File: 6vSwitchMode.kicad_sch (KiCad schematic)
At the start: 29 parts, among them IC1 TPS40192DRCT-TPS40192DRCT, Q1 BUK9M17-30EX / BUK7M10-40E, Q2 BUK9M17-30EX / BUK7M10-40E

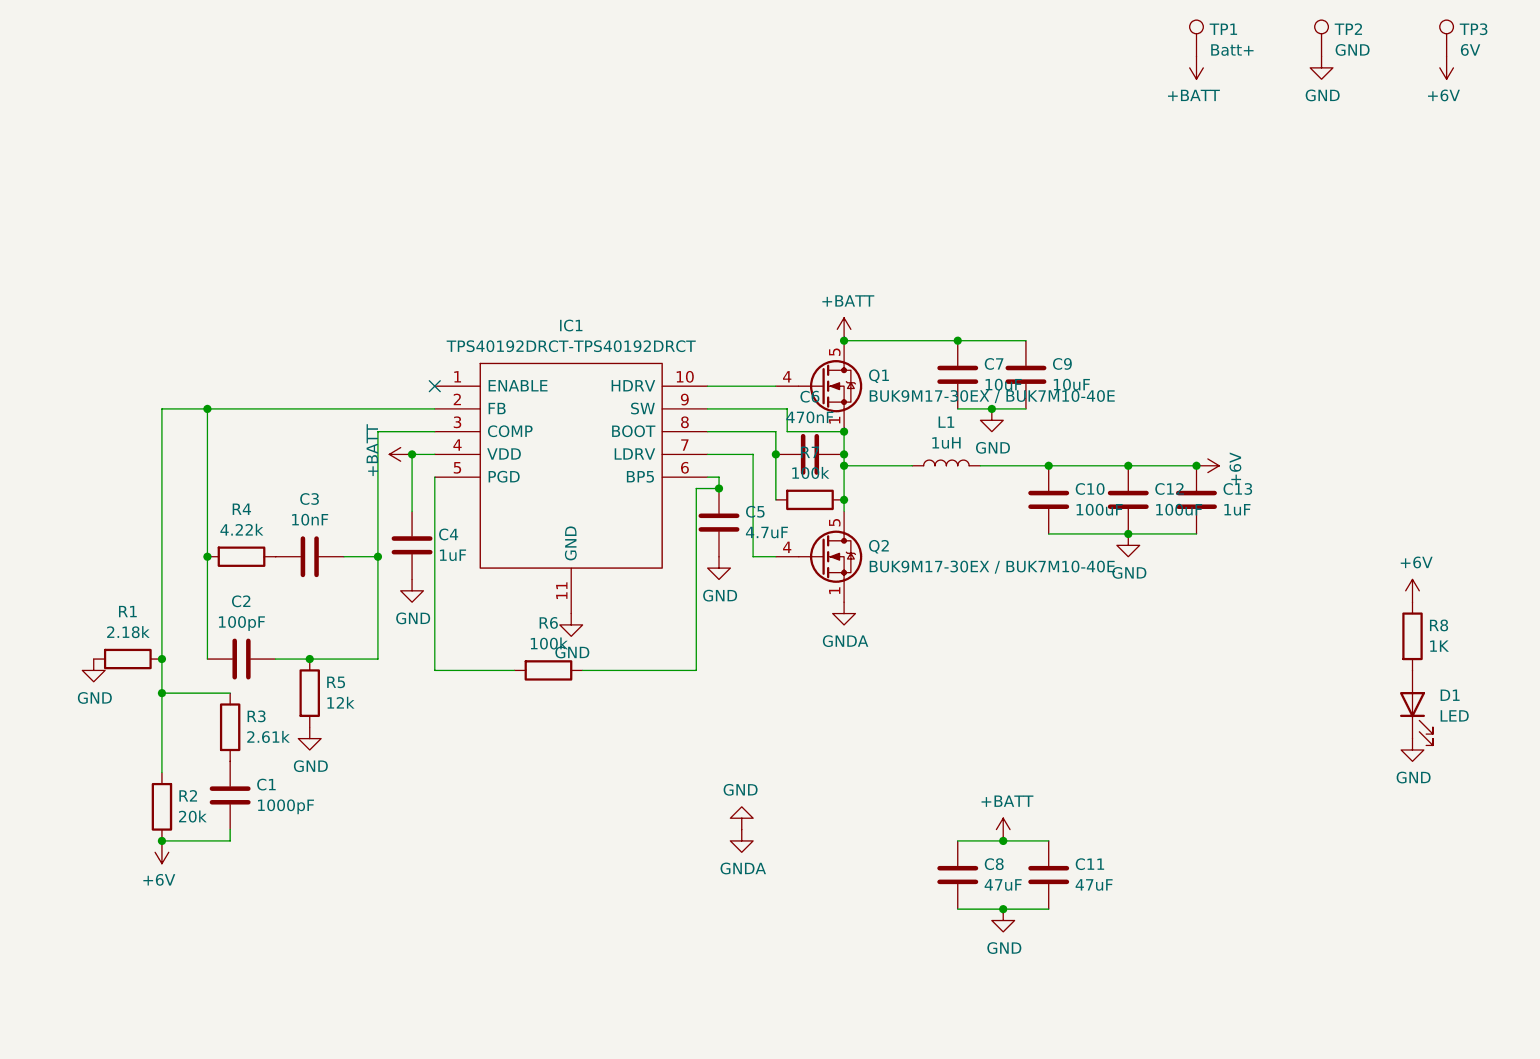
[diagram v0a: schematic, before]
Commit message: Initial layout and all parts added. Some pins still not connected to power
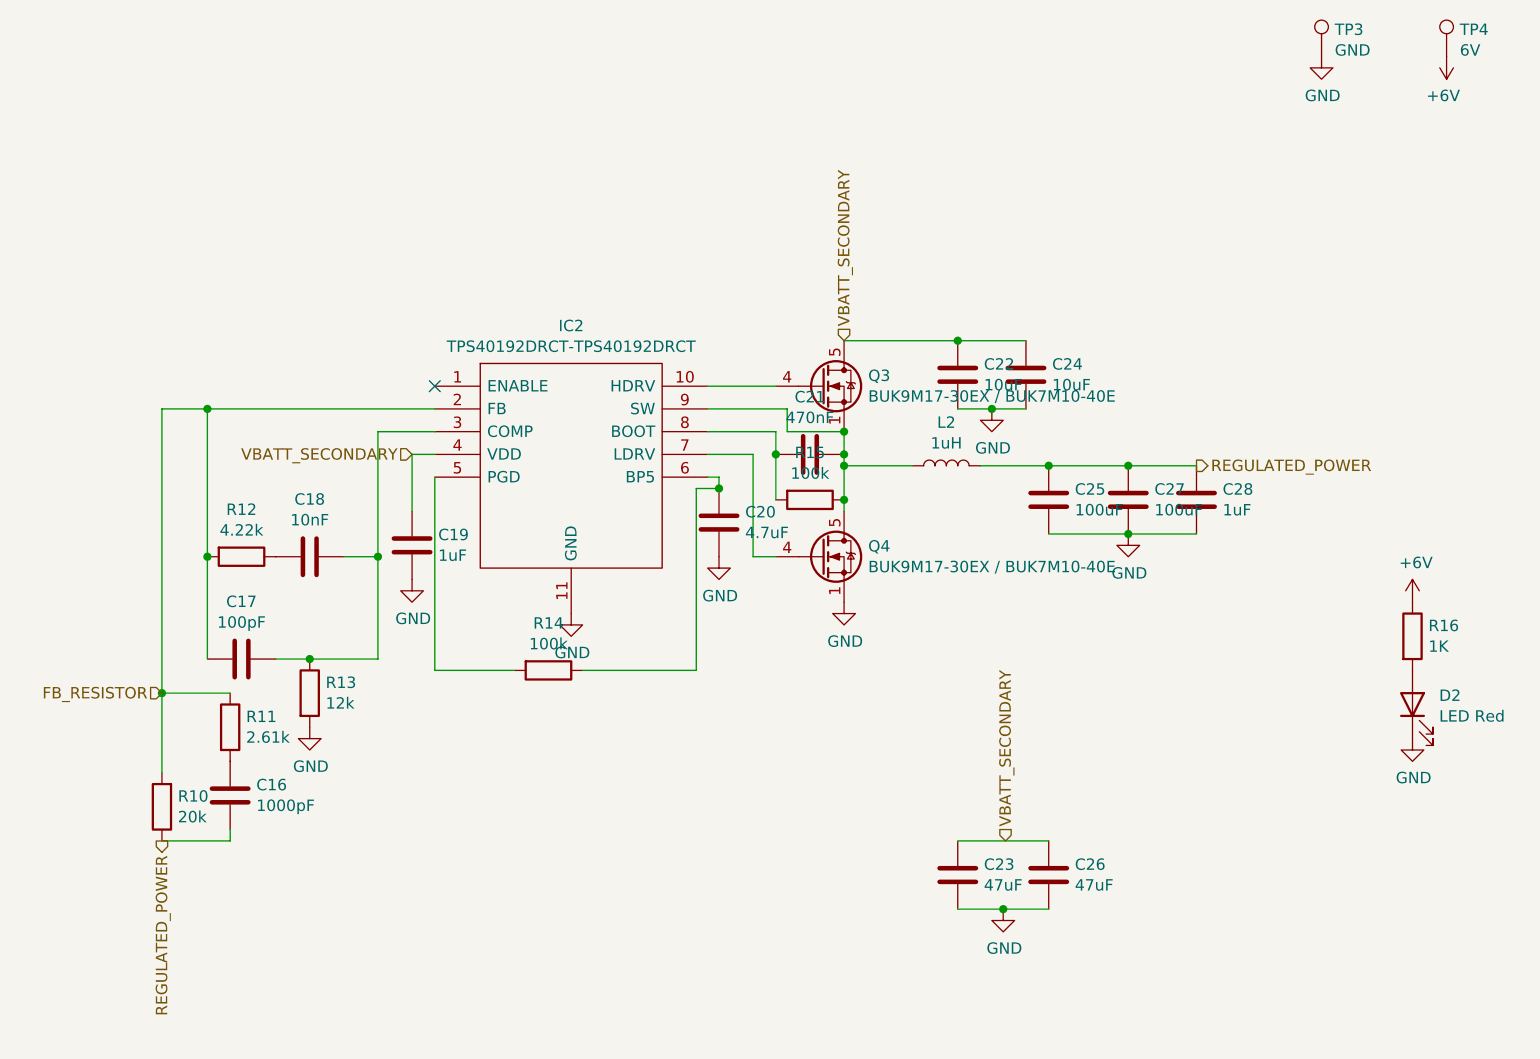
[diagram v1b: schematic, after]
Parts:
- removed R1: 2.18k, Resistor_SMD:R_0402_1005Metric, symbol Device:R
- removed TP1: Batt+, TestPoint:TestPoint_Pad_D2.5mm, symbol Connector:TestPoint
- D2: renamed from D1; value LED -> LED Red
- renumbered C1 to C16, C2 to C17, C3 to C18, C4 to C19, C5 to C20, C6 to C21, C7 to C22, C8 to C23, C9 to C24, C10 to C25, C11 to C26, C12 to C27, C13 to C28, IC1 to IC2, L1 to L2, Q1 to Q3, Q2 to Q4, R2 to R10, R3 to R11, R4 to R12, R5 to R13, R6 to R14, R7 to R15, R8 to R16, TP2 to TP3, TP3 to TP4
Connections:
- net +6V: no longer C16.1, C25.1, C27.1, C28.1, L2.2, R10.1
- net FB_RESISTOR: now reaches C17.2, IC2.2 (FB), R10.2, R11.1, R12.2
- net +BATT renamed VBATT_SECONDARY
- new net REGULATED_POWER: C16.1, C25.1, C27.1, C28.1, L2.2, R10.1

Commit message: Diff pairs routed
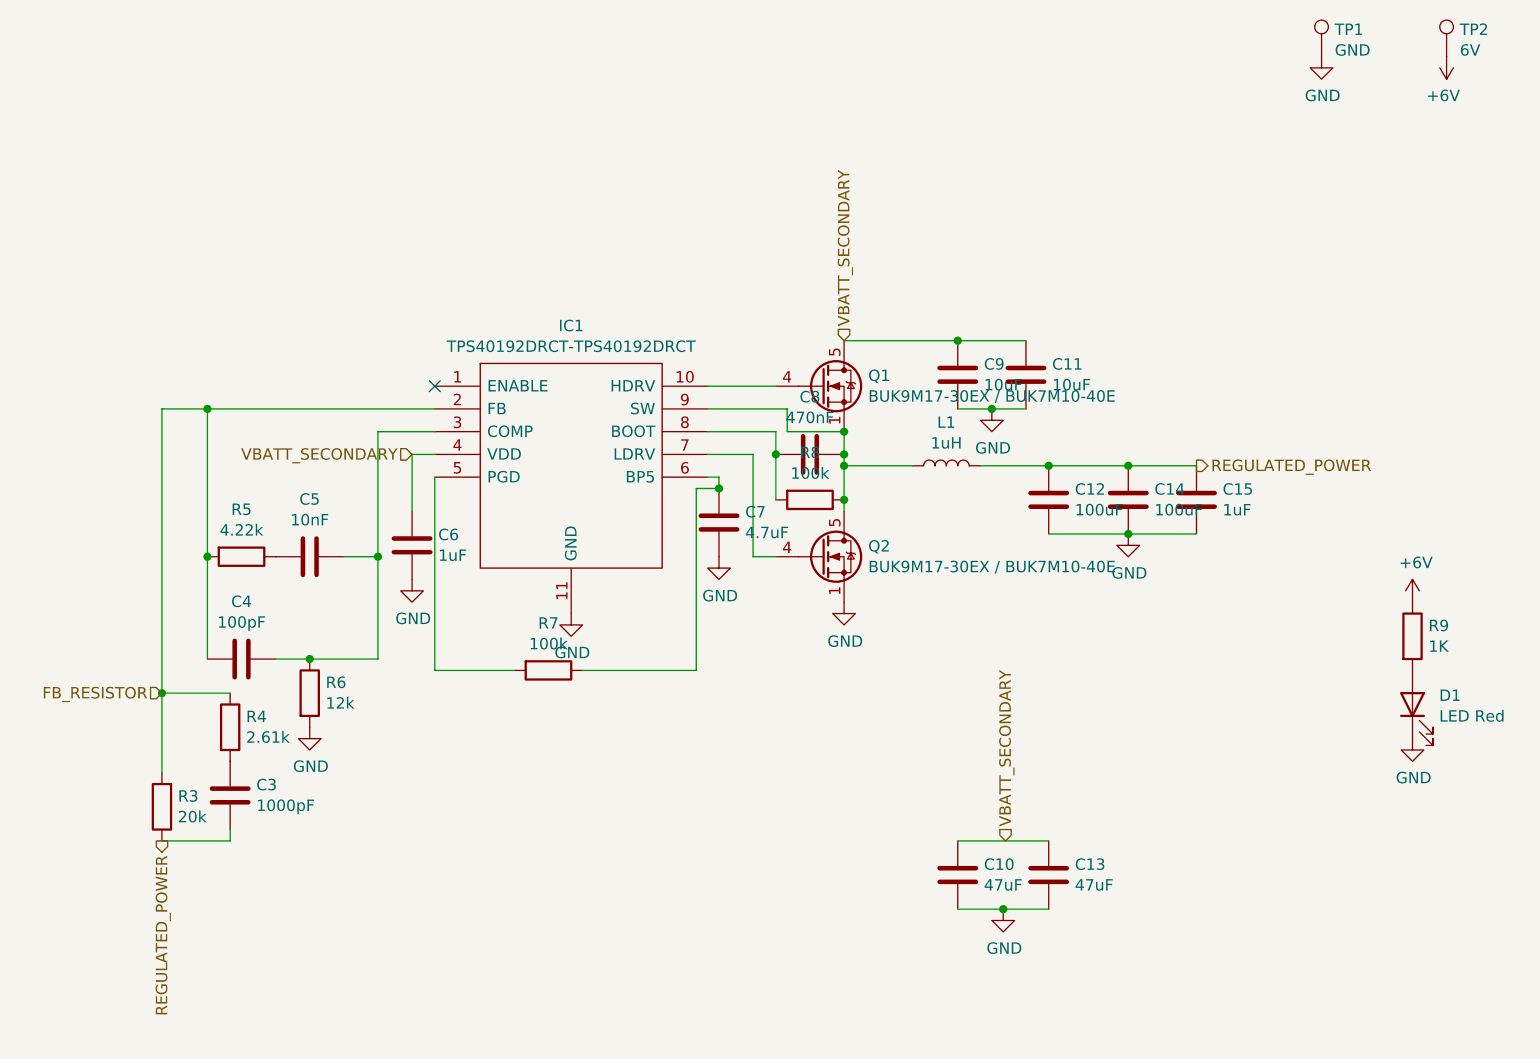
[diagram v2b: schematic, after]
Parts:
- renumbered C23 to C10, C24 to C11, C25 to C12, C26 to C13, C27 to C14, C28 to C15, C16 to C3, C17 to C4, C18 to C5, C19 to C6, C20 to C7, C21 to C8, C22 to C9, D2 to D1, IC2 to IC1, L2 to L1, Q3 to Q1, Q4 to Q2, R10 to R3, R11 to R4, R12 to R5, R13 to R6, R14 to R7, R15 to R8, R16 to R9, TP3 to TP1, TP4 to TP2

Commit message: mostly routed, need to add more layers fo power and finish low speed signal routing
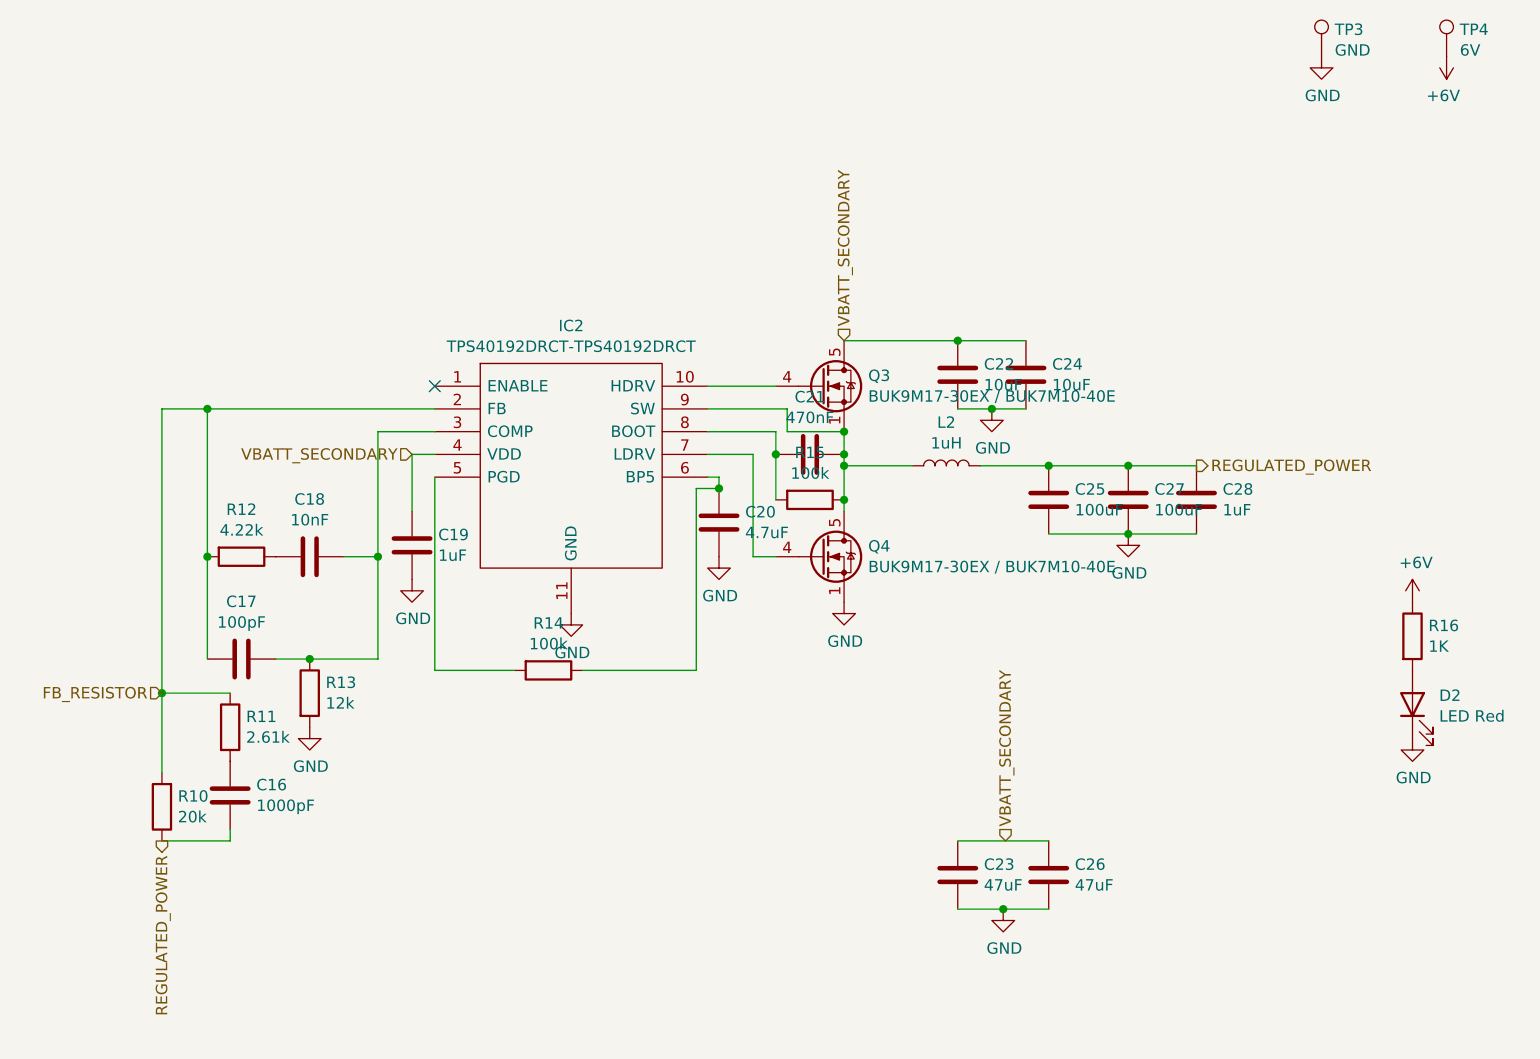
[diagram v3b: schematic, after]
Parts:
- renumbered C3 to C16, C4 to C17, C5 to C18, C6 to C19, C7 to C20, C8 to C21, C9 to C22, C10 to C23, C11 to C24, C12 to C25, C13 to C26, C14 to C27, C15 to C28, D1 to D2, IC1 to IC2, L1 to L2, Q1 to Q3, Q2 to Q4, R3 to R10, R4 to R11, R5 to R12, R6 to R13, R7 to R14, R8 to R15, R9 to R16, TP1 to TP3, TP2 to TP4

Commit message: Added usb to ethernet and changed mcu to stm32g4
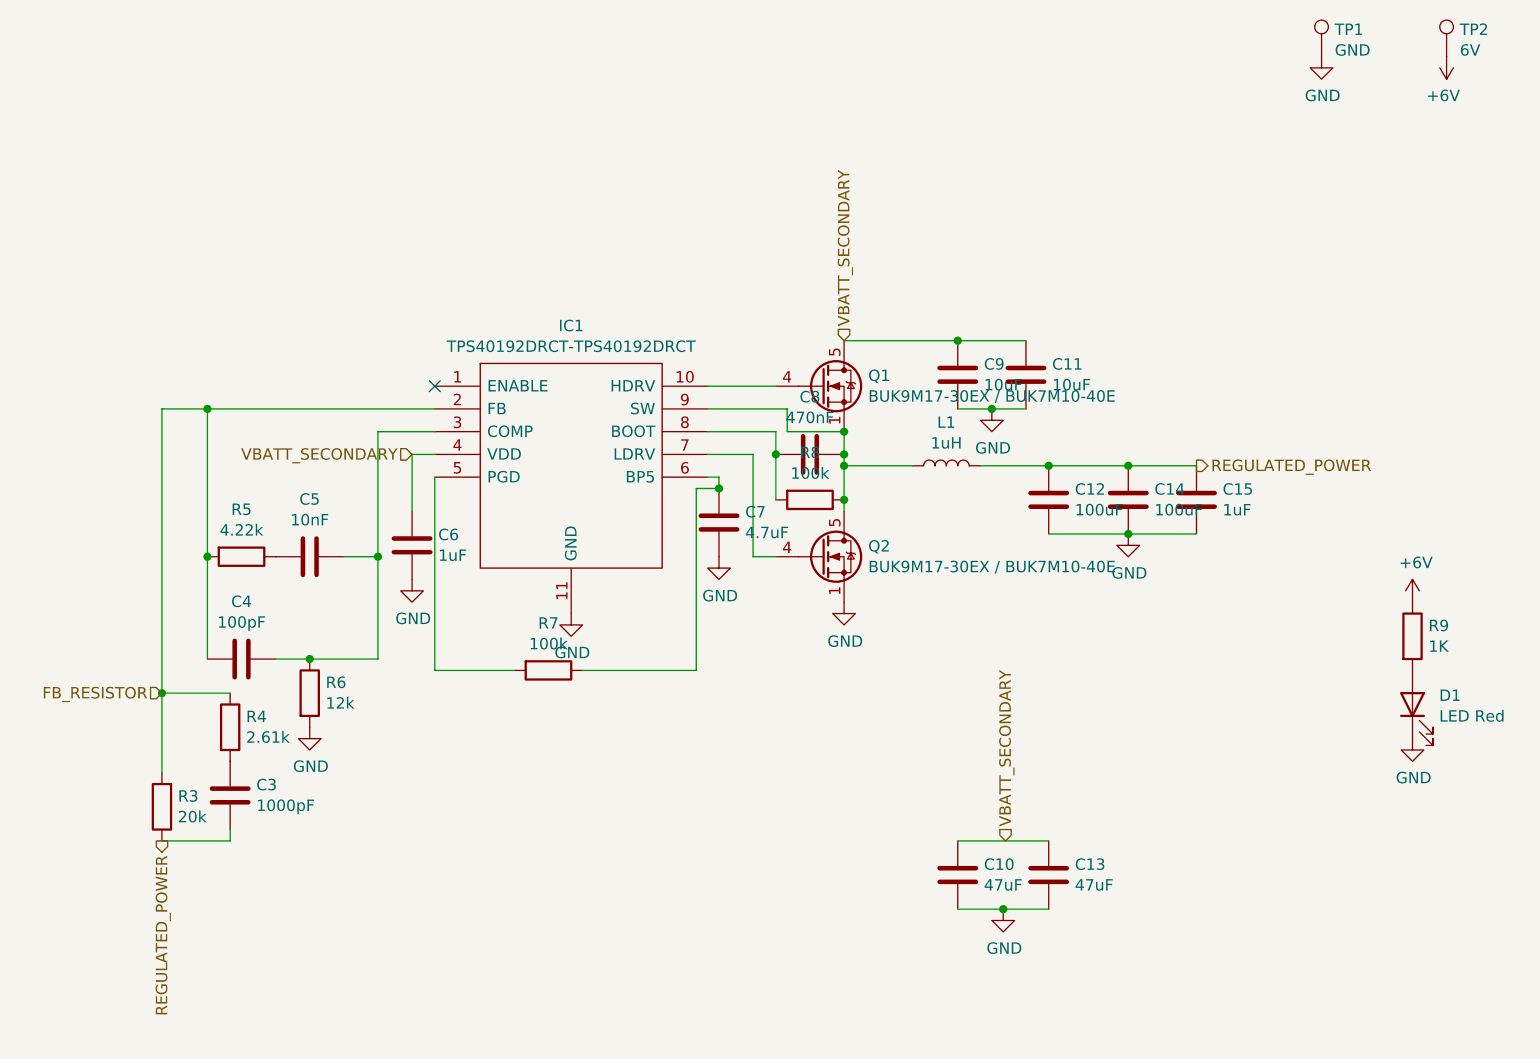
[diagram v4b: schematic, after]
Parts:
- renumbered C23 to C10, C24 to C11, C25 to C12, C26 to C13, C27 to C14, C28 to C15, C16 to C3, C17 to C4, C18 to C5, C19 to C6, C20 to C7, C21 to C8, C22 to C9, D2 to D1, IC2 to IC1, L2 to L1, Q3 to Q1, Q4 to Q2, R10 to R3, R11 to R4, R12 to R5, R13 to R6, R14 to R7, R15 to R8, R16 to R9, TP3 to TP1, TP4 to TP2

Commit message: added schematic PDF
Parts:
- renumbered C3 to C16, C4 to C17, C5 to C18, C6 to C19, C7 to C20, C8 to C21, C9 to C22, C10 to C23, C11 to C24, C12 to C25, C13 to C26, C14 to C27, C15 to C28, D1 to D2, IC1 to IC2, L1 to L2, Q1 to Q3, Q2 to Q4, R3 to R10, R4 to R11, R5 to R12, R6 to R13, R7 to R14, R8 to R15, R9 to R16, TP1 to TP3, TP2 to TP4
